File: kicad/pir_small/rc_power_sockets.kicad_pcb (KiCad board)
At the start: 2 copper layers, 25 x 25 mm, 28 parts, among them IC1 ATTINY85, J1 PIR, J2 433MHZ, P1 ICSP, P2 ALT_PWR, P3 CONN_01X01, P4 CONN_01X01, Q1 NMOS, Q2 PMOS, SW1 SWITCH_INV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

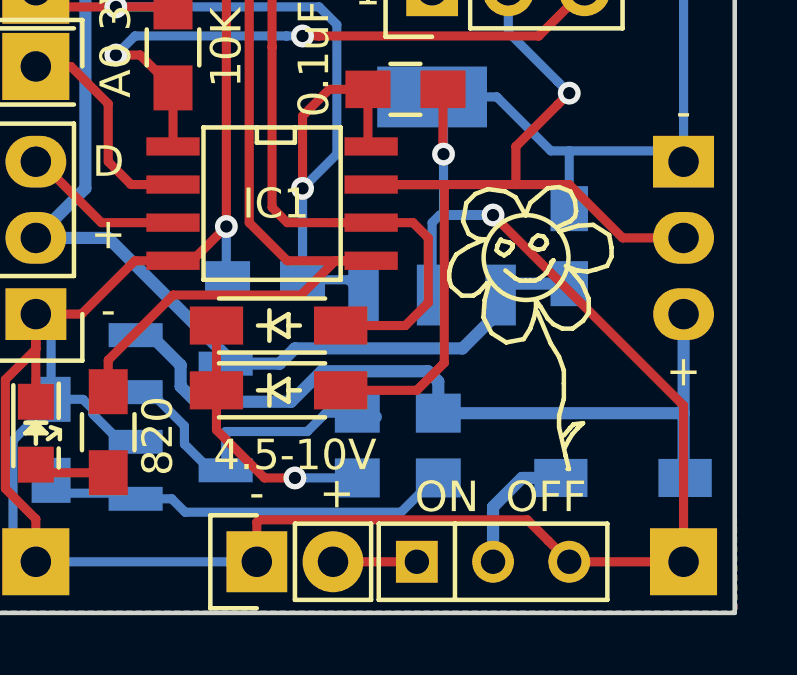
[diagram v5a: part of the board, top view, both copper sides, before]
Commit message: 10uF cap on the power input
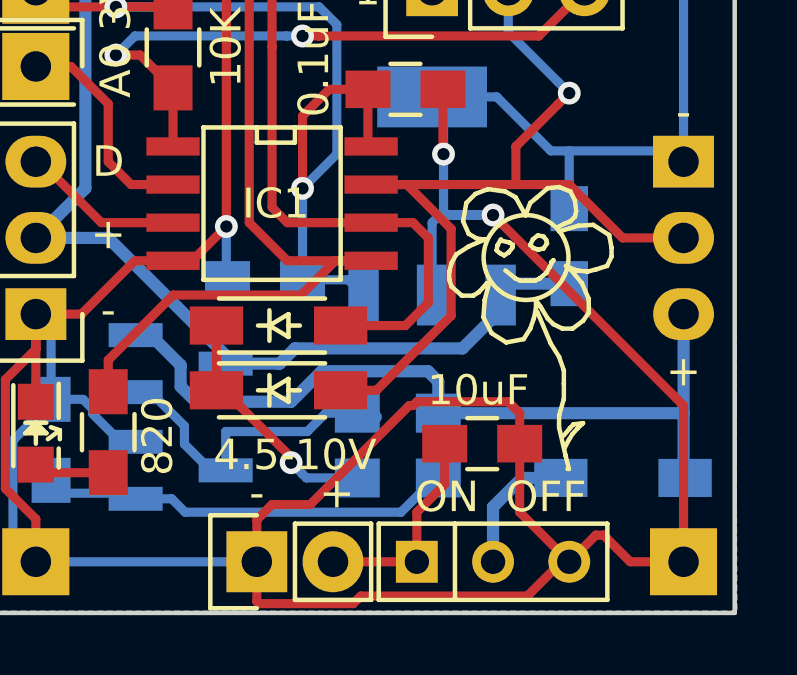
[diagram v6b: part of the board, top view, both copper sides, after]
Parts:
- added C4: 10uF, Capacitors_SMD:C_0805_HandSoldering, F.Cu at (164.0, 83.0)
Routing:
- net GND: track 123.2 -> 141.5 mm
- net /VCC: track 2.79 -> 7.12 mm
- net /SCK: track 31.7 -> 30.4 mm
- net /NBASE_ON: track 8.84 -> 8.17 mm
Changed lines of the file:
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@@
 (kicad_pcb (version 4) (host pcbnew 4.0.2-stable)
   (general
-    (links 49)
+    (links 51)
     (no_connects 0)
-    (area 144.000667 61.624 175.915334 93.082)
+    (area 147.382999 63.582999 172.533001 88.733001)
     (thickness 1.6)
     (drawings 34)
-    (tracks 205)
+    (tracks 226)
     (zones 0)
-    (modules 28)
+    (modules 29)
     (nets 17)
   )
@@
     (fp_circle (center -0.17 2.94) (end 0.83 1.94) (layer F.SilkS) (width 0.15))
   )
+  (module Capacitors_SMD:C_0805_HandSoldering (layer F.Cu)
+    (at 164.042 83.016)
+    (descr "Capacitor SMD 0805, hand soldering")
+    (tags "capacitor 0805")
+    (attr smd)
+    (fp_text reference C4 (at 0 -2.1) (layer F.SilkS) hide
+      (effects (font (size 1 1) (thickness 0.15)))
+    )
+    (fp_text value 10uF (at -0.127 -1.778) (layer F.SilkS)
+      (effects (font (size 1 1) (thickness 0.15)))
+    )
+    (fp_line (start -2.3 -1) (end 2.3 -1) (layer F.CrtYd) (width 0.05))
+    (fp_line (start -2.3 1) (end 2.3 1) (layer F.CrtYd) (width 0.05))
+    (fp_line (start -2.3 -1) (end -2.3 1) (layer F.CrtYd) (width 0.05))
+    (fp_line (start 2.3 -1) (end 2.3 1) (layer F.CrtYd) (width 0.05))
+    (fp_line (start 0.5 -0.85) (end -0.5 -0.85) (layer F.SilkS) (width 0.15))
+    (fp_line (start -0.5 0.85) (end 0.5 0.85) (layer F.SilkS) (width 0.15))
+    (pad 1 smd rect (at -1.25 0) (size 1.5 1.25) (layers F.Cu F.Paste F.Mask)
+      (net 16 /VCC))
+    (pad 2 smd rect (at 1.25 0) (size 1.5 1.25) (layers F.Cu F.Paste F.Mask)
+      (net 1 GND))
+    (model Capacitors_SMD.3dshapes/C_0805_HandSoldering.wrl
+      (at (xyz 0 0 0))
+      (scale (xyz 1 1 1))
+      (rotate (xyz 0 0 0))
+    )
+  )
   (gr_text "petermclarke\n@gmail.com" (at 155.767 65.363) (layer F.SilkS)
     (effects (font (size 0.762 0.762) (thickness 0.1524) italic))
@@
     (effects (font (size 1.016 1.016) (thickness 0.1524) italic) (justify mirror))
   )
+  (segment (start 170.753 86.953) (end 168.975 86.953) (width 0.3048) (layer F.Cu) (net 1))
+  (segment (start 168.975 86.953) (end 168.086 86.064) (width 0.3048) (layer F.Cu) (net 1))
+  (segment (start 168.086 86.064) (end 167.832 86.064) (width 0.3048) (layer F.Cu) (net 1))
+  (segment (start 167.832 86.064) (end 166.943 86.953) (width 0.3048) (layer F.Cu) (net 1))
+  (segment (start 159.739561 88.350001) (end 156.605201 88.350001) (width 0.3048) (layer F.Cu) (net 1))
+  (segment (start 156.529 88.2738) (end 156.529 86.953) (width 0.3048) (layer F.Cu) (net 1))
+  (segment (start 156.605201 88.350001) (end 156.529 88.2738) (width 0.3048) (layer F.Cu) (net 1))
+  (segment (start 165.292 83.016) (end 165.292 82) (width 0.3048) (layer F.Cu) (net 1))
+  (segment (start 165.292 82) (end 164.911 81.619) (width 0.3048) (layer F.Cu) (net 1))
+  (segment (start 161.736 81.746) (end 161.609 81.746) (width 0.3048) (layer F.Cu) (net 1))
+  (segment (start 164.911 81.619) (end 161.863 81.619) (width 0.3048) (layer F.Cu) (net 1))
+  (segment (start 161.863 81.619) (end 161.736 81.746) (width 0.3048) (layer F.Cu) (net 1))
+  (segment (start 161.609 81.746) (end 158.307 85.048) (width 0.3048) (layer F.Cu) (net 1))
+  (segment (start 158.307 85.048) (end 157.037 85.048) (width 0.3048) (layer F.Cu) (net 1))
+  (segment (start 157.037 85.048) (end 156.529 85.556) (width 0.3048) (layer F.Cu) (net 1))
+  (segment (start 156.529 85.556) (end 156.529 86.953) (width 0.3048) (layer F.Cu) (net 1))
+  (segment (start 165.292 83.016) (end 165.292 85.302) (width 0.3048) (layer F.Cu) (net 1))
+  (segment (start 165.292 85.302) (end 166.943 86.953) (width 0.3048) (layer F.Cu) (net 1))
+  (segment (start 159.739561 88.350001) (end 159.993562 88.096) (width 0.3048) (layer F.Cu) (net 1))
+  (segment (start 159.993562 88.096) (end 165.546 88.096) (width 0.3048) (layer F.Cu) (net 1))
+  (segment (start 165.546 88.096) (end 166.435 87.207) (width 0.3048) (layer F.Cu) (net 1))
+  (segment (start 166.435 87.207) (end 166.689 87.207) (width 0.3048) (layer F.Cu) (net 1))
+  (segment (start 166.689 87.207) (end 166.943 86.953) (width 0.3048) (layer F.Cu) (net 1))
   (segment (start 166.943 73.257) (end 166.328 73.257) (width 0.3048) (layer B.Cu) (net 1))
   (segment (start 166.328 73.257) (end 164.53 71.459) (width 0.3048) (layer B.Cu) (net 1))
@@
   (segment (start 162.371 78.571) (end 162.371 78.063) (width 0.3048) (layer B.Cu) (net 1))
   (segment (start 166.943 75.182) (end 166.943 73.257) (width 0.3048) (layer B.Cu) (net 1))
-  (segment (start 156.529 86.953) (end 156.529 85.6322) (width 0.3048) (layer F.Cu) (net 1))
-  (segment (start 156.529 85.6322) (end 156.605201 85.555999) (width 0.3048) (layer F.Cu) (net 1))
-  (segment (start 156.605201 85.555999) (end 165.545999 85.555999) (width 0.3048) (layer F.Cu) (net 1))
-  (segment (start 165.545999 85.555999) (end 166.244501 86.254501) (width 0.3048) (layer F.Cu) (net 1))
-  (segment (start 166.244501 86.254501) (end 166.943 86.953) (width 0.3048) (layer F.Cu) (net 1))
   (segment (start 156.529 86.953) (end 149.163 86.953) (width 0.3048) (layer B.Cu) (net 1))
   (segment (start 166.943 73.257) (end 170.392 73.257) (width 0.3048) (layer B.Cu) (net 1))
@@
   (segment (start 154.37 76.92) (end 155.513 75.777) (width 0.3048) (layer F.Cu) (net 1))
   (via (at 155.513 75.777) (size 0.762) (drill 0.4064) (layers F.Cu B.Cu) (net 1))
-  (segment (start 166.943 86.953) (end 170.753 86.953) (width 0.3048) (layer F.Cu) (net 1))
   (segment (start 149.163 86.953) (end 148.401 86.191) (width 0.3048) (layer B.Cu) (net 1))
   (segment (start 148.401 86.191) (end 148.401 82.909) (width 0.3048) (layer B.Cu) (net 1))
@@
   (segment (start 151.068 82.03552) (end 151.98748 82.955) (width 0.3048) (layer B.Cu) (net 1))
   (segment (start 151.98748 82.955) (end 152.48786 82.955) (width 0.3048) (layer B.Cu) (net 1))
+  (segment (start 160.5168 81.238) (end 159.323 81.238) (width 0.3048) (layer F.Cu) (net 2))
+  (segment (start 161.5328 74.38) (end 163.006 75.8532) (width 0.3048) (layer F.Cu) (net 2))
+  (segment (start 160.339 74.38) (end 161.5328 74.38) (width 0.3048) (layer F.Cu) (net 2))
+  (segment (start 163.006 78.7488) (end 160.5168 81.238) (width 0.3048) (layer F.Cu) (net 2))
+  (segment (start 163.006 75.8532) (end 163.006 78.7488) (width 0.3048) (layer F.Cu) (net 2))
   (segment (start 166.562001 70.951001) (end 166.943 71.332) (width 0.3048) (layer B.Cu) (net 2))
   (segment (start 164.911 69.3) (end 166.562001 70.951001) (width 0.3048) (layer B.Cu) (net 2))
@@
   (segment (start 170.6006 76.158) (end 170.753 76.158) (width 0.3048) (layer B.Cu) (net 2))
   (segment (start 164.911 67.903) (end 164.911 68.03) (width 0.3048) (layer F.Cu) (net 2))
-  (segment (start 160.339 74.38) (end 162.752 74.38) (width 0.3048) (layer F.Cu) (net 2))
-  (segment (start 162.752 74.38) (end 162.77741 74.40541) (width 0.3048) (layer F.Cu) (net 2))
-  (segment (start 162.77741 74.40541) (end 162.77741 80.32359) (width 0.3048) (layer F.Cu) (net 2))
-  (segment (start 162.77741 80.32359) (end 161.863 81.238) (width 0.3048) (layer F.Cu) (net 2))
-  (segment (start 161.863 81.238) (end 159.323 81.238) (width 0.3048) (layer F.Cu) (net 2))
   (segment (start 166.943 74.38) (end 168.721 76.158) (width 0.3048) (layer F.Cu) (net 2))
   (segment (start 168.721 76.158) (end 170.753 76.158) (width 0.3048) (layer F.Cu) (net 2))
@@
   (segment (start 155.49014 83.20015) (end 155.49014 83.905) (width 0.3048) (layer B.Cu) (net 11))
   (segment (start 160.399 82.127) (end 160.499 82.127) (width 0.4064) (layer B.Cu) (net 11))
-  (segment (start 155.1828 81.238) (end 155.1828 82.5588) (width 0.3048) (layer F.Cu) (net 12))
-  (segment (start 155.1828 82.5588) (end 156.782994 84.158994) (width 0.3048) (layer F.Cu) (net 12))
-  (segment (start 156.782994 84.158994) (end 157.799 84.158994) (width 0.3048) (layer F.Cu) (net 12))
-  (segment (start 157.799006 84.159) (end 157.799 84.158994) (width 0.3048) (layer B.Cu) (net 12))
-  (segment (start 159.878 84.159) (end 157.799006 84.159) (width 0.3048) (layer B.Cu) (net 12))
-  (via (at 157.799 84.158994) (size 0.762) (drill 0.4064) (layers F.Cu B.Cu) (net 12))
+  (segment (start 158.052999 84.031999) (end 157.672 83.651) (width 0.3048) (layer B.Cu) (net 12))
+  (segment (start 158.18 84.159) (end 158.052999 84.031999) (width 0.3048) (layer B.Cu) (net 12))
+  (segment (start 159.878 84.159) (end 158.18 84.159) (width 0.3048) (layer B.Cu) (net 12))
+  (segment (start 157.672 83.4732) (end 157.672 83.651) (width 0.3048) (layer F.Cu) (net 12))
+  (segment (start 155.1828 81.238) (end 155.4368 81.238) (width 0.3048) (layer F.Cu) (net 12))
+  (segment (start 155.4368 81.238) (end 157.672 83.4732) (width 0.3048) (layer F.Cu) (net 12))
+  (via (at 157.672 83.651) (size 0.762) (drill 0.4064) (layers F.Cu B.Cu) (net 12))
   (segment (start 155.1828 79.079) (end 155.1828 81.238) (width 0.3048) (layer F.Cu) (net 12))
   (segment (start 162.578 82) (end 162.578 80.9436) (width 0.4064) (layer B.Cu) (net 13))
@@
   (segment (start 164.403 85.965172) (end 164.403 86.953) (width 0.4064) (layer B.Cu) (net 15))
   (segment (start 166.6636 84.159) (end 166.4096 84.159) (width 0.3048) (layer B.Cu) (net 15))
+  (segment (start 162.792 84.373) (end 161.863 85.302) (width 0.3048) (layer F.Cu) (net 16))
+  (segment (start 161.863 85.302) (end 161.863 86.953) (width 0.3048) (layer F.Cu) (net 16))
+  (segment (start 162.792 83.016) (end 162.792 84.373) (width 0.3048) (layer F.Cu) (net 16))
   (segment (start 159.069 86.953) (end 161.863 86.953) (width 0.3048) (layer F.Cu) (net 16))
   (zone (net 1) (net_name GND) (layer B.Cu) (hatch edge 0.508)

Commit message: Tiny logo
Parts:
- added REF**: TheApiLogoTiny, theapi_footprints:TheApiLogoTiny, F.Cu at (170.8, 66.6)
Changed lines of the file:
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@@
-(kicad_pcb (version 4) (host pcbnew 4.0.2-stable)
+(kicad_pcb (version 4) (host pcbnew 4.0.1-stable)
   (general
-    (links 51)
+    (links 0)
     (no_connects 0)
     (area 147.382999 63.582999 172.533001 88.733001)
@@
     (tracks 226)
     (zones 0)
-    (modules 29)
+    (modules 30)
     (nets 17)
   )
@@
     )
   )
+  (module theapi_footprints:TheApiLogoTiny (layer F.Cu)
+    (at 170.753 66.633)
+    (fp_text reference REF** (at 0 0.5) (layer F.SilkS) hide
+      (effects (font (size 1 1) (thickness 0.15)))
+    )
+    (fp_text value TheApiLogoTiny (at 0 -0.5) (layer F.Fab) hide
+      (effects (font (size 1 1) (thickness 0.15)))
+    )
+    (fp_line (start 0.26 4.07) (end 0.42 3.55) (layer F.Mask) (width 0.1016))
+    (fp_line (start 0.3 3.85) (end 0.26 4.07) (layer F.Mask) (width 0.1016))
+    (fp_line (start 0.18 3.57) (end 0.3 3.85) (layer F.Mask) (width 0.1016))
+    (fp_line (start -0.04 3.27) (end 0.18 3.57) (layer F.Mask) (width 0.1016))
+    (fp_line (start -0.13 2.84) (end -0.04 3.27) (layer F.Mask) (width 0.1016))
+    (fp_line (start 0.24 2.85) (end 0.24 2.68) (layer F.Mask) (width 0.1016))
+    (fp_line (start 0.26 2.95) (end 0.24 2.85) (layer F.Mask) (width 0.1016))
+    (fp_line (start 0.21 3.04) (end 0.26 2.95) (layer F.Mask) (width 0.1016))
+    (fp_line (start 0.09 3.07) (end 0.21 3.04) (layer F.Mask) (width 0.1016))
+    (fp_line (start -0.03 2.94) (end 0.09 3.07) (layer F.Mask) (width 0.1016))
+    (fp_line (start -0.1 2.75) (end -0.03 2.94) (layer F.Mask) (width 0.1016))
+    (fp_line (start 0.42 2.75) (end 0.33 2.62) (layer F.Mask) (width 0.1016))
+    (fp_line (start 0.55 2.78) (end 0.42 2.75) (layer F.Mask) (width 0.1016))
+    (fp_line (start 0.66 2.74) (end 0.55 2.78) (layer F.Mask) (width 0.1016))
+    (fp_line (start 0.7 2.64) (end 0.66 2.74) (layer F.Mask) (width 0.1016))
+    (fp_line (start 0.7 2.5) (end 0.7 2.64) (layer F.Mask) (width 0.1016))
+    (fp_line (start 0.6 2.36) (end 0.7 2.5) (layer F.Mask) (width 0.1016))
+    (fp_line (start 0.42 2.25) (end 0.6 2.36) (layer F.Mask) (width 0.1016))
+    (fp_line (start 0.52 2.22) (end 0.42 2.22) (layer F.Mask) (width 0.1016))
+    (fp_line (start 0.67 2.21) (end 0.52 2.22) (layer F.Mask) (width 0.1016))
+    (fp_line (start 0.77 2.14) (end 0.67 2.21) (layer F.Mask) (width 0.1016))
+    (fp_line (start 0.75 1.99) (end 0.77 2.14) (layer F.Mask) (width 0.1016))
+    (fp_line (start 0.64 1.89) (end 0.75 1.99) (layer F.Mask) (width 0.1016))
+    (fp_line (start 0.27 1.9) (end 0.64 1.89) (layer F.Mask) (width 0.1016))
+    (fp_line (start 0.39 1.77) (end 0.3 1.91) (layer F.Mask) (width 0.1016))
+    (fp_line (start 0.41 1.66) (end 0.39 1.77) (layer F.Mask) (width 0.1016))
+    (fp_line (start 0.36 1.55) (end 0.41 1.66) (layer F.Mask) (width 0.1016))
+    (fp_line (start 0.19 1.52) (end 0.36 1.55) (layer F.Mask) (width 0.1016))
+    (fp_line (start 0.03 1.58) (end 0.19 1.52) (layer F.Mask) (width 0.1016))
+    (fp_line (start -0.06 1.85) (end 0.03 1.58) (layer F.Mask) (width 0.1016))
+    (fp_line (start -0.16 2.76) (end -0.17 2.73) (layer F.Mask) (width 0.1016))
+    (fp_line (start -0.13 2.74) (end -0.16 2.76) (layer F.Mask) (width 0.1016))
+    (fp_line (start -0.15 2.76) (end -0.13 2.74) (layer F.Mask) (width 0.1016))
+    (fp_line (start -0.17 2.87) (end -0.15 2.76) (layer F.Mask) (width 0.1016))
+    (fp_line (start -0.23 2.98) (end -0.17 2.87) (layer F.Mask) (width 0.1016))
+    (fp_line (start -0.35 3.02) (end -0.23 2.98) (layer F.Mask) (width 0.1016))
+    (fp_line (start -0.46 2.98) (end -0.35 3.02) (layer F.Mask) (width 0.1016))
+    (fp_line (start -0.47 2.79) (end -0.46 2.98) (layer F.Mask) (width 0.1016))
+    (fp_line (start -0.39 2.59) (end -0.47 2.79) (layer F.Mask) (width 0.1016))
+    (fp_line (start -0.66 2.63) (end -0.41 2.57) (layer F.Mask) (width 0.1016))
+    (fp_line (start -0.78 2.55) (end -0.66 2.63) (layer F.Mask) (width 0.1016))
+    (fp_line (start -0.82 2.42) (end -0.78 2.55) (layer F.Mask) (width 0.1016))
+    (fp_line (start -0.73 2.27) (end -0.82 2.42) (layer F.Mask) (width 0.1016))
+    (fp_line (start -0.46 2.22) (end -0.73 2.27) (layer F.Mask) (width 0.1016))
+    (fp_line (start -0.68 2.1) (end -0.47 2.15) (layer F.Mask) (width 0.1016))
+    (fp_line (start -0.79 1.93) (end -0.68 2.1) (layer F.Mask) (width 0.1016))
+    (fp_line (start -0.68 1.74) (end -0.79 1.93) (layer F.Mask) (width 0.1016))
+    (fp_line (start -0.4 1.67) (end -0.68 1.74) (layer F.Mask) (width 0.1016))
+    (fp_line (start -0.13 1.81) (end -0.4 1.67) (layer F.Mask) (width 0.1016))
+    (fp_line (start 0.04 2.48) (end 0.16 2.39) (layer F.Mask) (width 0.0762))
+    (fp_line (start -0.09 2.49) (end 0.04 2.48) (layer F.Mask) (width 0.0762))
+    (fp_line (start -0.21 2.42) (end -0.09 2.49) (layer F.Mask) (width 0.0762))
+    (fp_circle (center -0.16 2.2) (end -0.13 2.21) (layer F.Mask) (width 0.15))
+    (fp_circle (center -0.02 2.28) (end 0.39 2.28) (layer F.Mask) (width 0.127))
+    (fp_circle (center 0.12 2.2) (end 0.15 2.21) (layer F.Mask) (width 0.15))
+  )
   (gr_text "petermclarke\n@gmail.com" (at 155.767 65.363) (layer F.SilkS)
